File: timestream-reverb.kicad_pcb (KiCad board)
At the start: 2 copper layers, 81.8 x 86.4 mm, 43 parts, among them J1 Conn_01x01_Female, J2 Conn_01x01_Female, J3 Conn_01x01_Female, J4 Conn_01x01_Female, J5 Conn_01x01_Female, SW1 SW_SPDT, U1 L78L05_TO92, U2 TL072, U3 TL072, U4 BTDR-2

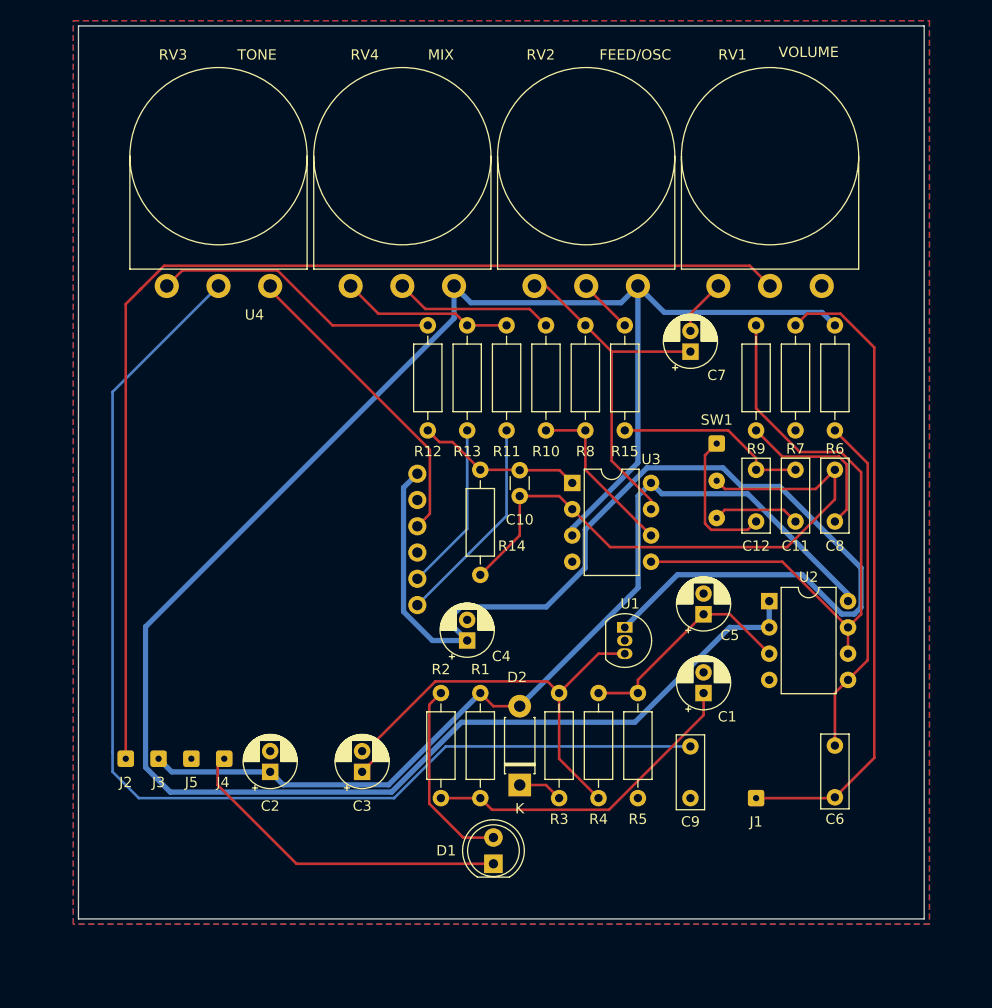
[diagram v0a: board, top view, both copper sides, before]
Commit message: fix: Improve layout and remove wires to PCB
The following has been fixed:
  - Wires are no longer wired to the PCB
  - PCB size is smaller
  - LED is not included in the layout
  - BTDR-2 is not included in the layout
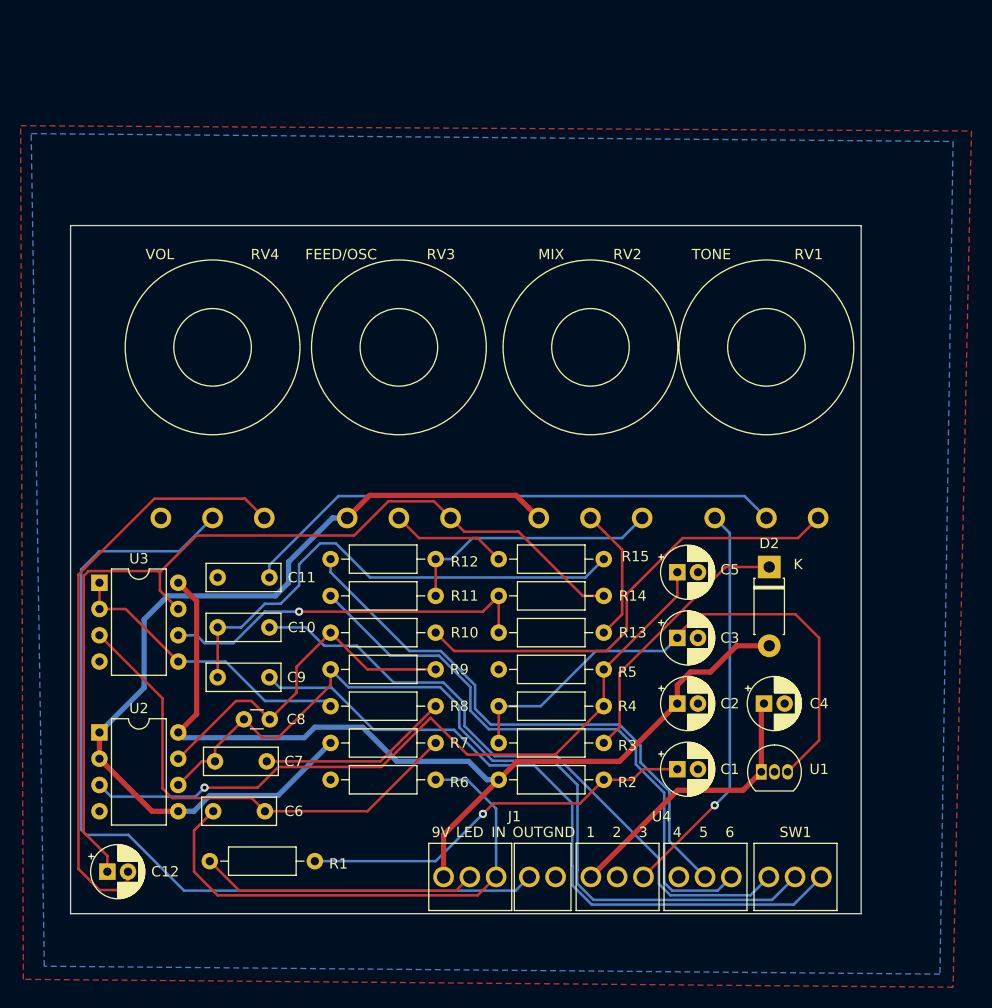
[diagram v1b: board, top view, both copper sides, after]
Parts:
- removed D1: LED, LED_THT:LED_D5.0mm
- removed J2, J3, J4, J5: Conn_01x01_Female, Connector_Wire:SolderWire-0.1sqmm_1x01_D0.4mm_OD1mm
- C10: value 100p -> 4.7n; footprint Capacitor_THT:C_Disc_D3.0mm_W1.6mm_P2.50mm -> Capacitor_THT:C_Rect_L7.0mm_W2.5mm_P5.00mm
- C11: value 22n -> 33n
- C12: value 4.7n -> 1u; footprint Capacitor_THT:C_Rect_L7.0mm_W2.5mm_P5.00mm -> Capacitor_THT:CP_Radial_D5.0mm_P2.00mm
- C7: value 1u -> 22n; footprint Capacitor_THT:CP_Radial_D5.0mm_P2.00mm -> Capacitor_THT:C_Rect_L7.0mm_W2.5mm_P5.00mm
- C8: value 22n -> 100p; footprint Capacitor_THT:C_Rect_L7.0mm_W2.5mm_P5.00mm -> Capacitor_THT:C_Disc_D3.0mm_W1.6mm_P2.50mm
- C9: value 33n -> 22n
- J1: value Conn_01x01_Female -> Conn_01x05_Female; footprint Connector_Wire:SolderWire-0.1sqmm_1x01_D0.4mm_OD1mm -> timestream-reverb:TerminalBlock_5pin_2.54mm
- R10: value 10k -> 1k
- R12: value 1k -> 10k
- R8: value 22k -> 10k
- R9: value 10k -> 22k
- RV1, RV3: footprint Potentiometer_THT:Potentiometer_Omeg_PC16BU_Vertical -> timestream-reverb:Tayda_Potentiometer
- RV2: value 10kb -> 25kb; footprint Potentiometer_THT:Potentiometer_Omeg_PC16BU_Vertical -> timestream-reverb:Tayda_Potentiometer
- RV4: value 25kb -> 10kb; footprint Potentiometer_THT:Potentiometer_Omeg_PC16BU_Vertical -> timestream-reverb:Tayda_Potentiometer
- SW1: footprint Connector_Wire:SolderWire-0.1sqmm_1x03_P3.6mm_D0.4mm_OD1mm -> timestream-reverb:TerminalBlock_3pin_2.54mm
- U4: footprint timestream-reverb:BTDR-2H -> timestream-reverb:TerminalBlock_6pin_2.54mm
- moved C12 73.8 mm to (110.0, 124.0), turned to 0 degrees
- moved U2 66.0 mm to (109.2, 110.5)
- moved C8 62.0 mm to (123.2, 109.2), turned to 0 degrees
- moved C7 60.7 mm to (120.4, 113.3), turned to 0 degrees
- moved R7 60.4 mm to (131.6, 111.5), turned to 0 degrees
- moved R6 58.5 mm to (141.7, 115.1), turned to 180 degrees
- moved C11 56.8 mm to (120.7, 95.5), turned to 0 degrees
- moved C6 55.5 mm to (125.2, 118.1), turned to 180 degrees
- moved R9 52.9 mm to (131.6, 104.4), turned to 0 degrees
- moved U4 52.0 mm to (163.6, 124.5), turned to 0 degrees
- moved C9 47.2 mm to (120.7, 105.2), turned to 0 degrees
- moved U3 46.7 mm to (109.2, 96.0)
- moved R8 44.3 mm to (131.6, 108.0), turned to 0 degrees
- moved SW1 42.6 mm to (176.5, 124.5), turned to 0 degrees
- moved C2 39.9 mm to (165.1, 107.7), turned to 0 degrees
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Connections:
- C11 pad 1: Net-(C11-Pad1) -> GND
- C12 pad 1: Net-(C11-Pad1) -> Net-(C12-Pad1)
- C8 pad 1: Net-(C10-Pad1) -> Net-(C7-Pad1)
- C9 pad 1: GND -> Net-(C10-Pad1)
- J1 pad 1: IN -> +9V
- R1 pad 1: Net-(D1-Pad2) -> LED+
- R10 pad 1: Net-(R10-Pad1) -> Net-(C8-Pad2)
- R12 pad 1: Net-(C10-Pad2) -> Net-(R12-Pad1)
- R12 pad 2: Net-(R12-Pad2) -> Net-(R11-Pad2)
- R13 pad 2: Net-(R11-Pad2) -> Net-(R13-Pad2)
- R14 pad 1: Net-(C10-Pad1) -> Net-(C12-Pad1)
- R14 pad 2: Net-(C10-Pad2) -> Net-(R13-Pad1)
- R15 pad 2: Net-(C11-Pad1) -> Net-(C10-Pad1)
- R6 pad 1: VB -> IN
- R6 pad 2: Net-(C6-Pad1) -> GND
- R7 pad 1: IN -> VB
- R7 pad 2: GND -> Net-(C6-Pad1)
- R8 pad 1: Net-(C7-Pad1) -> Net-(R8-Pad1)
- R8 pad 2: Net-(R10-Pad1) -> Net-(C7-Pad2)
- R9 pad 1: Net-(R9-Pad1) -> Net-(C7-Pad1)
- RV1 pad 1: GND -> Net-(RV1-Pad1)
- RV1 pad 2: OUT -> Net-(C11-Pad2)
- RV1 pad 3: Net-(C7-Pad2) -> Net-(R10-Pad2)
- RV2 pad 2: Net-(R15-Pad1) -> Net-(R13-Pad2)
- RV2 pad 3: Net-(C7-Pad1) -> Net-(R11-Pad2)
- RV3 pad 1: Net-(RV3-Pad1) -> VB
- RV3 pad 2: Net-(C9-Pad2) -> Net-(R15-Pad1)
- RV3 pad 3: Net-(R12-Pad2) -> Net-(C12-Pad1)
- RV4 pad 1: VB -> GND
- RV4 pad 2: Net-(R10-Pad2) -> OUT
- RV4 pad 3: Net-(R11-Pad2) -> Net-(C12-Pad2)
- SW1 pad 1: Net-(C12-Pad2) -> Net-(C10-Pad2)
- SW1 pad 2: Net-(C10-Pad1) -> Net-(C7-Pad1)
- SW1 pad 3: Net-(C11-Pad2) -> Net-(C9-Pad2)
- U2 pad 5: Net-(C6-Pad1) -> VB
- U2 pad 6: Net-(R9-Pad1) -> Net-(C7-Pad1)
- U2 pad 7: Net-(R9-Pad1) -> Net-(C8-Pad2)
- U3 pad 1: Net-(C10-Pad2) -> Net-(R8-Pad1)
- U3 pad 2: Net-(C10-Pad1) -> Net-(R8-Pad1)
- U3 pad 3: VB -> Net-(C6-Pad1)
- U3 pad 5: Net-(R9-Pad1) -> Net-(R8-Pad1)
- U3 pad 6: Net-(R10-Pad1) -> Net-(R13-Pad1)
- U3 pad 7: Net-(C7-Pad1) -> Net-(C12-Pad1)
- U4 pad 3: Net-(RV3-Pad1) -> Net-(RV1-Pad1)
- U4 pad 5: Net-(R13-Pad1) -> Net-(R12-Pad1)
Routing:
- net VB: track 195.9 -> 87.7 mm
- net Net-(C12-Pad1): track 0.00 -> 91.0 mm
- net +5V: track 106.3 -> 27.4 mm
- net Net-(R9-Pad1): track 60.5 -> 0.00 mm
- net Net-(R12-Pad1): track 0.00 -> 54.8 mm
- net Net-(C7-Pad1): track 34.5 -> 84.4 mm
- net Net-(C5-Pad1): track 22.0 -> 71.7 mm, vias 0 -> 1
- net Net-(C10-Pad2): track 16.1 -> 62.5 mm
- net Net-(C11-Pad2): track 8.41 -> 52.9 mm
- net Net-(C12-Pad2): track 13.7 -> 57.1 mm
- net Net-(C9-Pad2): track 110.3 -> 68.2 mm
- net Net-(RV1-Pad1): track 0.00 -> 38.8 mm, vias 0 -> 1
- net Net-(R11-Pad1): track 20.5 -> 58.5 mm
- net FS: track 32.4 -> 0.00 mm
- net Net-(RV3-Pad1): track 30.1 -> 0.00 mm
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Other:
- board size 81.8 x 86.4 mm -> 76.5 x 66.5 mm
- board text added: "1"
- board text added: "2"
- board text added: "3"
- board text added: "4"
- board text added: "5"
- board text added: "6"
- board text added: "9V"
- board text added: "GND"
- board text added: "IN"
- board text added: "LED"
- board text added: "OUT"
- board text added: "VOL"
- board text added: "timestream_reverb_v1"
- board text removed: "VOLUME"
